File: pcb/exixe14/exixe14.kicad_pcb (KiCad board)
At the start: 2 copper layers, 47 parts, among them J1 Conn_01x07, J2 Conn_01x07, Q1 Q_PNP_BEC, Q10 Q_NPN_BEC, Q11 Q_NPN_BEC, Q12 Q_NPN_BEC, Q13 Q_NPN_BEC, Q14 Q_NPN_BEC, Q2 Q_NPN_BEC, Q3 Q_NPN_BEC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

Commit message: updating exixe14 pcb
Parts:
- moved C2 110.7 mm to (52.2, 76.8)
- moved D1 102.3 mm to (60.0, 64.9)
- moved C3 101.3 mm to (65.0, 85.6), turned to 180 degrees
- moved Q11 99.8 mm to (53.1, 69.7)
- moved Q12 99.7 mm to (52.1, 66.9)
- moved Q13 99.0 mm to (52.1, 64.2)
- moved Q14 98.4 mm to (52.5, 61.5)
- moved Q8 95.3 mm to (52.4, 72.5)
- moved Q9 91.4 mm to (55.0, 57.8), turned to 180 degrees
- moved C1 91.3 mm to (66.4, 54.4), turned to 180 degrees
- moved Q2 89.7 mm to (52.3, 55.0)
- moved R15 87.0 mm to (53.6, 84.2), turned to -90 degrees
- moved R25 85.8 mm to (51.8, 58.2), turned to -90 degrees
- moved Q1 84.3 mm to (57.7, 52.4), turned to 90 degrees
- moved Q10 84.1 mm to (62.8, 56.0), turned to 90 degrees
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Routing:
- net +3.3V: track 0.00 -> 56.9 mm, vias 0 -> 2
- net /PWM_RED: track 0.00 -> 24.8 mm, vias 0 -> 2
- net /PWM_GREEN: track 0.00 -> 19.7 mm, vias 0 -> 2
- net /PWM_BLUE: track 0.00 -> 17.3 mm, vias 0 -> 2
- net /SPI_CS: track 0.00 -> 14.0 mm, vias 0 -> 2
- net /SWD_CLK: track 0.00 -> 13.9 mm, vias 0 -> 1
- net /SWD_DIO: track 0.00 -> 12.8 mm, vias 0 -> 1
- net /NRST: track 0.00 -> 10.7 mm, vias 0 -> 1
- net Net-(J1-Pin_7): track 0.00 -> 10.2 mm
- net HV: track 0.00 -> 9.57 mm, vias 0 -> 1
- net Net-(U1-PB6): track 0.00 -> 8.19 mm
- net /SPI_SCK: track 0.00 -> 5.83 mm
- net /NIXIE_1: track 0.00 -> 5.71 mm
- net Net-(Q5-B): track 0.00 -> 5.25 mm
- net /NIXIE_LEFT: track 0.00 -> 5.18 mm
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
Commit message: pcb layout is hard
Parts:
- moved R23 34.6 mm to (34.2, 72.7), turned to 180 degrees
- moved R24 33.7 mm to (34.2, 74.7), turned to 180 degrees
- moved R25 26.8 mm to (34.2, 78.5), turned to 180 degrees
- moved R2 25.2 mm to (74.0, 82.1), turned to 180 degrees
- moved R19 24.4 mm to (65.0, 55.2), turned to 90 degrees
- moved R21 22.7 mm to (39.0, 81.5)
- moved R5 22.3 mm to (41.3, 81.5)
- moved R17 22.2 mm to (52.3, 57.2), turned to 180 degrees
- moved R1 22.0 mm to (74.0, 84.0), turned to 180 degrees
- moved R15 21.9 mm to (74.0, 76.2), turned to 0 degrees
- moved R8 21.7 mm to (47.0, 85.7), turned to 180 degrees
- moved Q8 19.6 mm to (62.6, 55.8), turned to -90 degrees
- moved R18 18.8 mm to (56.6, 58.1), turned to 90 degrees
- moved R22 18.2 mm to (68.5, 58.1), turned to -90 degrees
- moved Q10 17.6 mm to (54.9, 71.7), turned to 0 degrees
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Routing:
- net +3.3V: track 56.9 -> 3.24 mm, vias 2 -> 0
- net /PWM_RED: track 24.8 -> 0.00 mm, vias 2 -> 0
- net /PWM_GREEN: track 19.7 -> 0.00 mm, vias 2 -> 0
- net /PWM_BLUE: track 17.3 -> 0.00 mm, vias 2 -> 0
- net HV: track 9.57 -> 20.8 mm
- net /NRST: track 10.7 -> 0.00 mm, vias 1 -> 0
- net Net-(U1-PB6): track 8.19 -> 0.00 mm
- net /NIXIE_1: track 5.71 -> 0.00 mm
- net Net-(Q5-B): track 5.25 -> 0.00 mm
- net /NIXIE_LEFT: track 5.18 -> 0.00 mm
- net Net-(Q9-B): track 5.08 -> 0.00 mm
- net /STM_1: track 4.69 -> 0.00 mm
- net /NIXIE_RIGHT: track 4.32 -> 0.00 mm
- net /STM_7: track 3.66 -> 0.00 mm
- net /NIXIE_2: track 3.01 -> 0.00 mm
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
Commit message: working on exixe14 pcb
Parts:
- moved R23 34.7 mm to (67.8, 63.8), turned to 0 degrees
- moved R24 34.4 mm to (67.7, 82.4), turned to 0 degrees
- moved R25 33.5 mm to (67.7, 80.3), turned to 0 degrees
- moved R20 31.9 mm to (70.2, 73.5), turned to 90 degrees
- moved R16 27.1 mm to (54.5, 85.7), turned to 180 degrees
- moved R5 25.1 mm to (65.7, 75.4)
- moved R21 24.9 mm to (62.8, 74.3), turned to 0 degrees
- moved R8 23.3 mm to (67.8, 75.4), turned to 90 degrees
- moved R1 23.2 mm to (51.9, 76.9), turned to -90 degrees
- moved R15 22.7 mm to (52.5, 83.5), turned to 180 degrees
- moved R2 21.6 mm to (52.5, 79.7), turned to 0 degrees
- moved R10 16.9 mm to (73.5, 72.9)
- moved R7 15.9 mm to (59.9, 74.2)
- moved R14 7.23 mm to (52.0, 72.0), turned to 90 degrees
- moved C2 0.68 mm to (54.8, 76.3), turned to 0 degrees
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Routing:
- net +3.3V: track 3.24 -> 31.9 mm
- net /STM_6: track 0.00 -> 28.6 mm, vias 0 -> 2
- net /STM_5: track 0.00 -> 28.6 mm, vias 0 -> 2
- net Net-(Q5-B): track 0.00 -> 26.2 mm, vias 0 -> 2
- net /PWM_RED: track 0.00 -> 25.2 mm, vias 0 -> 2
- net /STM_8: track 0.00 -> 23.1 mm, vias 0 -> 2
- net Net-(Q4-B): track 0.00 -> 20.5 mm, vias 0 -> 2
- net /PWM_GREEN: track 0.00 -> 20.1 mm, vias 0 -> 2
- net /PWM_BLUE: track 0.00 -> 17.7 mm, vias 0 -> 2
- net /STM_1: track 0.00 -> 12.9 mm, vias 0 -> 2
- net /NRST: track 0.00 -> 10.1 mm, vias 0 -> 2
- net /NIXIE_LEFT: track 0.00 -> 4.73 mm
- net Net-(U1-PF0): track 0.00 -> 4.52 mm
- net Net-(Q3-B): track 0.00 -> 3.34 mm
- net /STM_LEFT: track 0.00 -> 3.06 mm
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
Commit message: layout is hard
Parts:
- moved R10 13.6 mm to (59.9, 74.1), turned to -90 degrees
- moved R21 7.90 mm to (54.9, 74.2), turned to 180 degrees
- moved R20 7.44 mm to (62.8, 74.5), turned to 0 degrees
- moved R7 2.08 mm to (57.8, 74.1)
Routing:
- net +3.3V: track 31.9 -> 0.00 mm
- net /STM_6: track 28.6 -> 0.00 mm, vias 2 -> 0
- net /STM_5: track 28.6 -> 0.00 mm, vias 2 -> 0
- net Net-(Q5-B): track 26.2 -> 0.00 mm, vias 2 -> 0
- net /PWM_RED: track 25.2 -> 0.00 mm, vias 2 -> 0
- net /STM_8: track 23.1 -> 0.00 mm, vias 2 -> 0
- net Net-(Q4-B): track 20.5 -> 0.00 mm, vias 2 -> 0
- net /PWM_GREEN: track 20.1 -> 0.00 mm, vias 2 -> 0
- net /PWM_BLUE: track 17.7 -> 0.00 mm, vias 2 -> 0
- net /SWD_DIO: track 14.5 -> 0.00 mm, vias 1 -> 0
- net HV: track 20.8 -> 6.92 mm
- net /SPI_CS: track 13.3 -> 0.00 mm, vias 1 -> 0
- net /SWD_CLK: track 13.1 -> 0.00 mm, vias 1 -> 0
- net /STM_1: track 12.9 -> 0.00 mm, vias 2 -> 0
- net /NRST: track 10.1 -> 0.00 mm, vias 2 -> 0
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
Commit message: This layout looks okay?
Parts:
- moved R8 24.2 mm to (51.4, 57.6)
- moved R23 21.3 mm to (68.3, 85.0), turned to -90 degrees
- moved R15 14.1 mm to (52.6, 69.4)
- moved R7 10.5 mm to (63.6, 65.3)
- moved R21 4.26 mm to (59.0, 73.0), turned to 90 degrees
- moved R10 3.69 mm to (63.6, 74.4), turned to 180 degrees
- moved R14 3.61 mm to (54.5, 74.6), turned to 180 degrees
- moved Q7 3.53 mm to (56.0, 57.7), turned to 180 degrees
- moved R18 3.44 mm to (59.6, 56.4), turned to 180 degrees
- moved Q3 3.18 mm to (52.8, 72.0)
- moved R5 3.09 mm to (67.0, 78.2), turned to 180 degrees
- moved R20 2.41 mm to (60.9, 73.0), turned to 90 degrees
- moved Q11 2.29 mm to (66.3, 60.7)
- moved R1 2.24 mm to (52.9, 78.9), turned to 0 degrees
- moved Q12 2.05 mm to (67.7, 63.4)
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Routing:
- net +3.3V: track 0.00 -> 71.8 mm, vias 0 -> 3
- net Net-(U1-PA12): track 0.00 -> 34.2 mm, vias 0 -> 2
- net /STM_6: track 0.00 -> 30.8 mm, vias 0 -> 2
- net /STM_4: track 0.00 -> 30.3 mm, vias 0 -> 2
- net /STM_5: track 0.00 -> 30.2 mm, vias 0 -> 2
- net Net-(Q5-B): track 0.00 -> 27.8 mm, vias 0 -> 2
- net Net-(Q12-B): track 0.00 -> 27.4 mm, vias 0 -> 2
- net /PWM_RED: track 0.00 -> 26.4 mm, vias 0 -> 2
- net /STM_7: track 0.00 -> 25.7 mm, vias 0 -> 2
- net /STM_2: track 0.00 -> 20.7 mm, vias 0 -> 2
- net /PWM_GREEN: track 0.00 -> 20.6 mm, vias 0 -> 2
- net Net-(Q13-B): track 0.00 -> 20.4 mm, vias 0 -> 2
- net /PWM_BLUE: track 0.00 -> 18.4 mm, vias 0 -> 2
- net Net-(U1-PB6): track 0.00 -> 17.4 mm, vias 0 -> 2
- net /SWD_CLK: track 0.00 -> 14.3 mm, vias 0 -> 1
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- added copper zone on B.Cu, net GND
- added copper zone on F.Cu, net GND

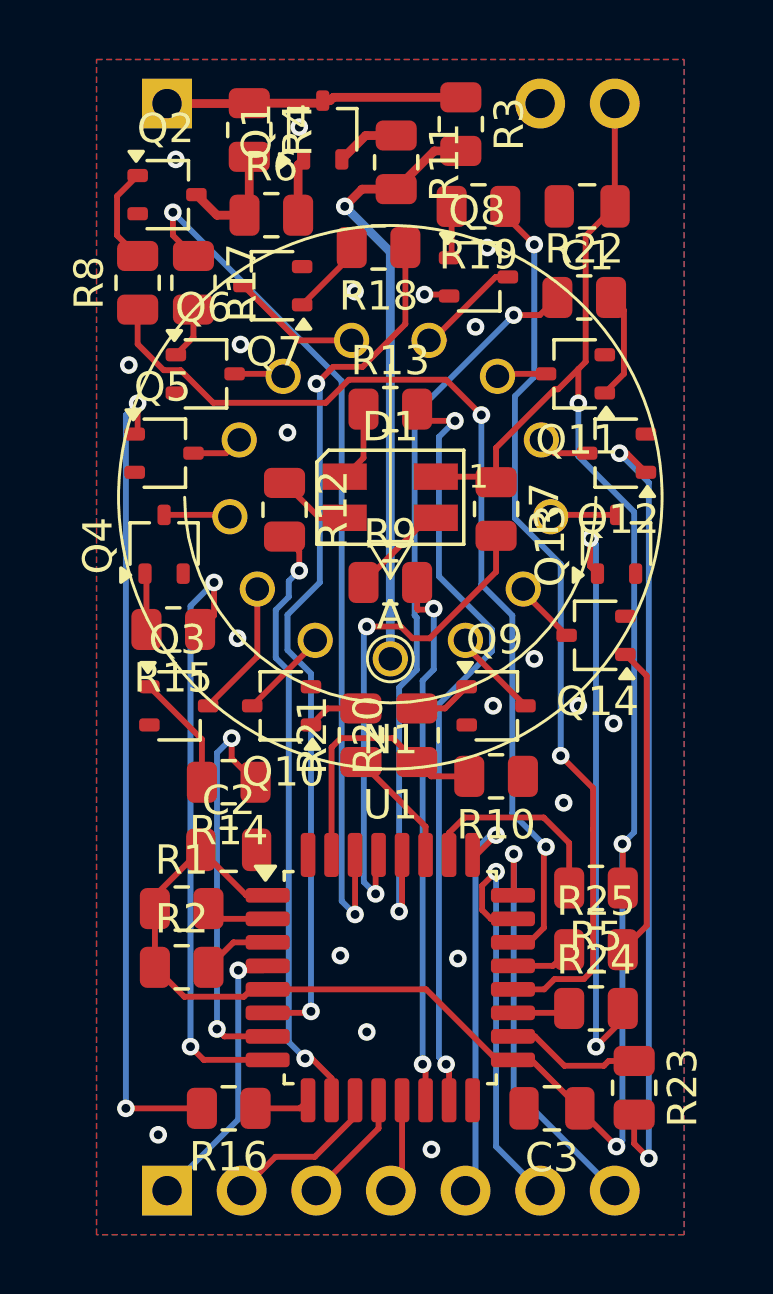
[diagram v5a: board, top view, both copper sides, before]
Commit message: attempt to correct firmware to remove glowing led issue
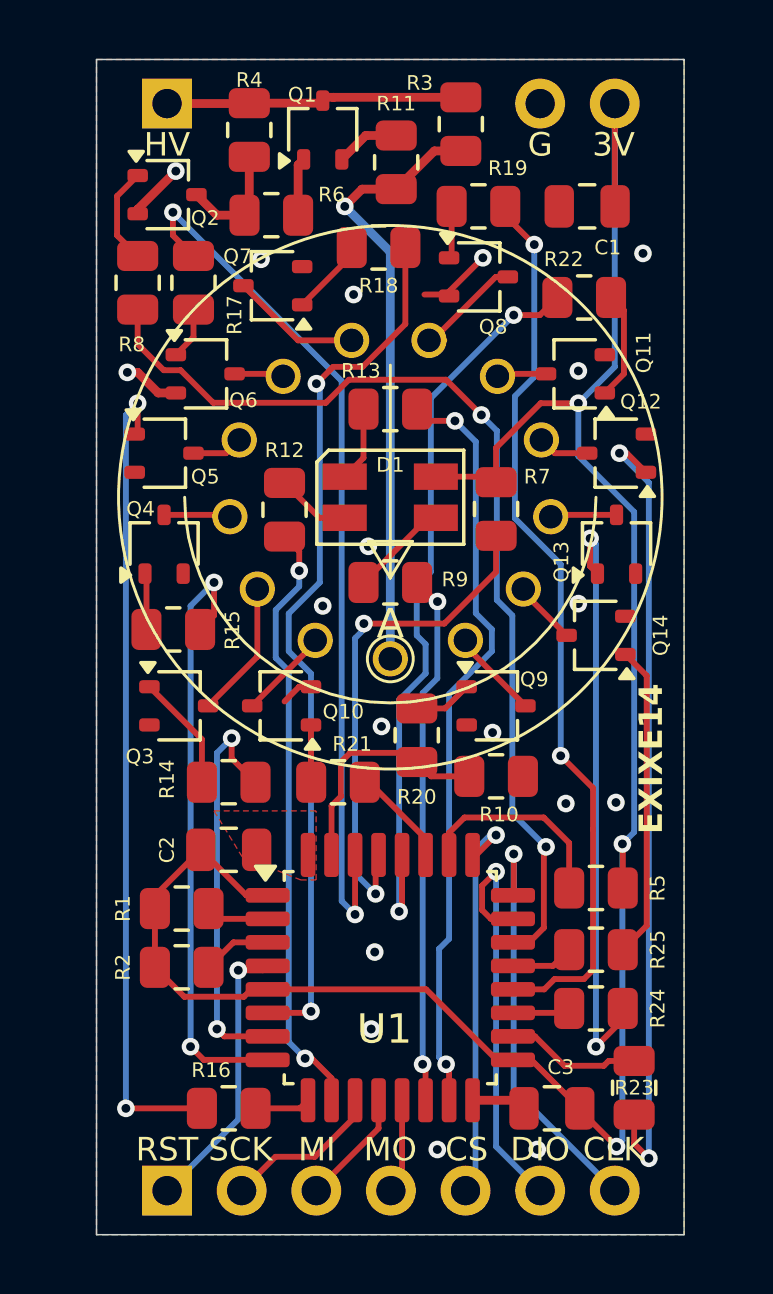
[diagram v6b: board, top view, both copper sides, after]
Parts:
- moved R21 1.78 mm to (58.2, 74.6), turned to 180 degrees
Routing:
- net GND: track 0.86 -> 10.0 mm, vias 20 -> 18
- net +3.3V: track 71.8 -> 74.8 mm
- net /STM_RIGHT: track 9.02 -> 8.12 mm
- net /STM_LEFT: track 4.07 -> 3.42 mm
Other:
- board outline added: 20 x 40 mm
- board text added: "3V"
- board text added: "CLK"
- board text added: "CS"
- board text added: "DIO"
- board text added: "EXIXE14"
- board text added: "G"
- board text added: "HV"
- board text added: "MI"
- board text added: "MO"
- board text added: "RST"
- board text added: "SCK"
